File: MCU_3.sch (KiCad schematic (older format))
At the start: 18 parts, among them U2 STM32F051K6Ux

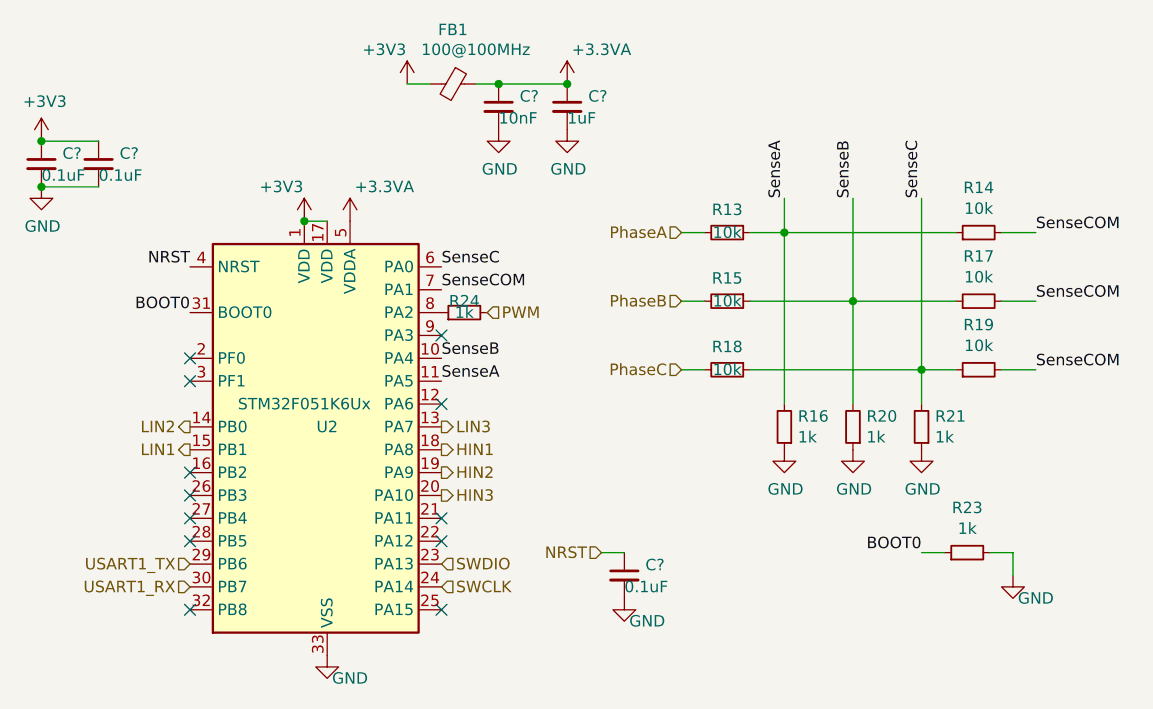
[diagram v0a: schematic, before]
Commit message: Added the rest of the phases and their associated components
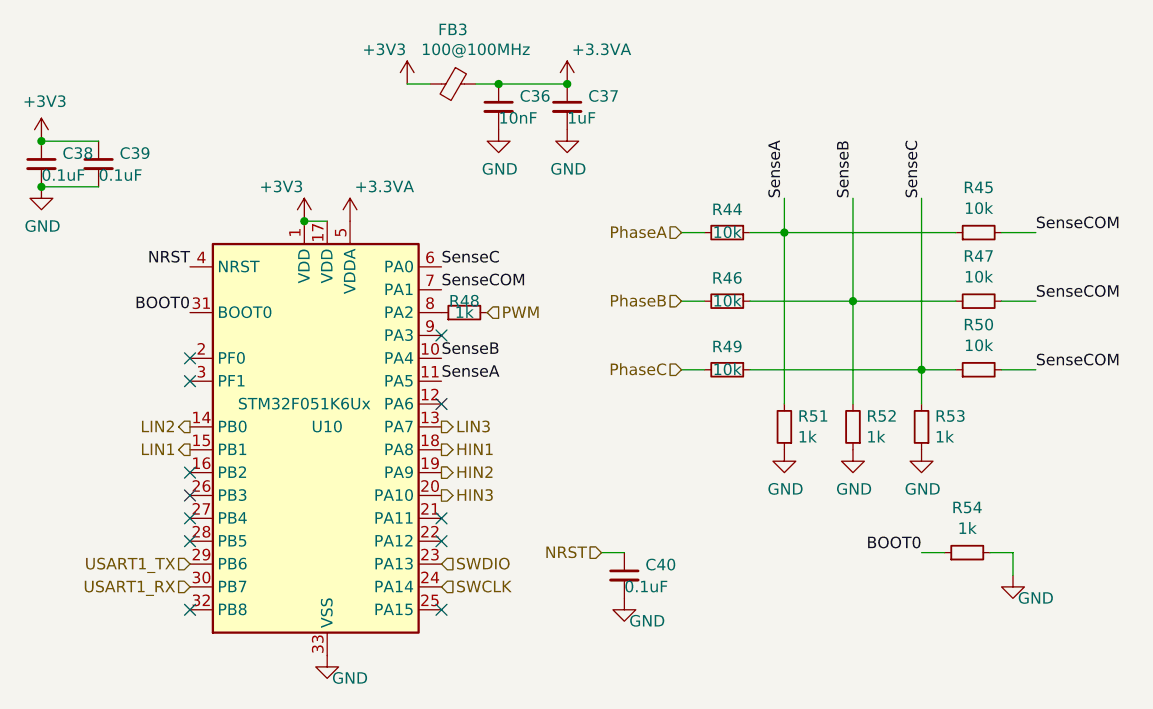
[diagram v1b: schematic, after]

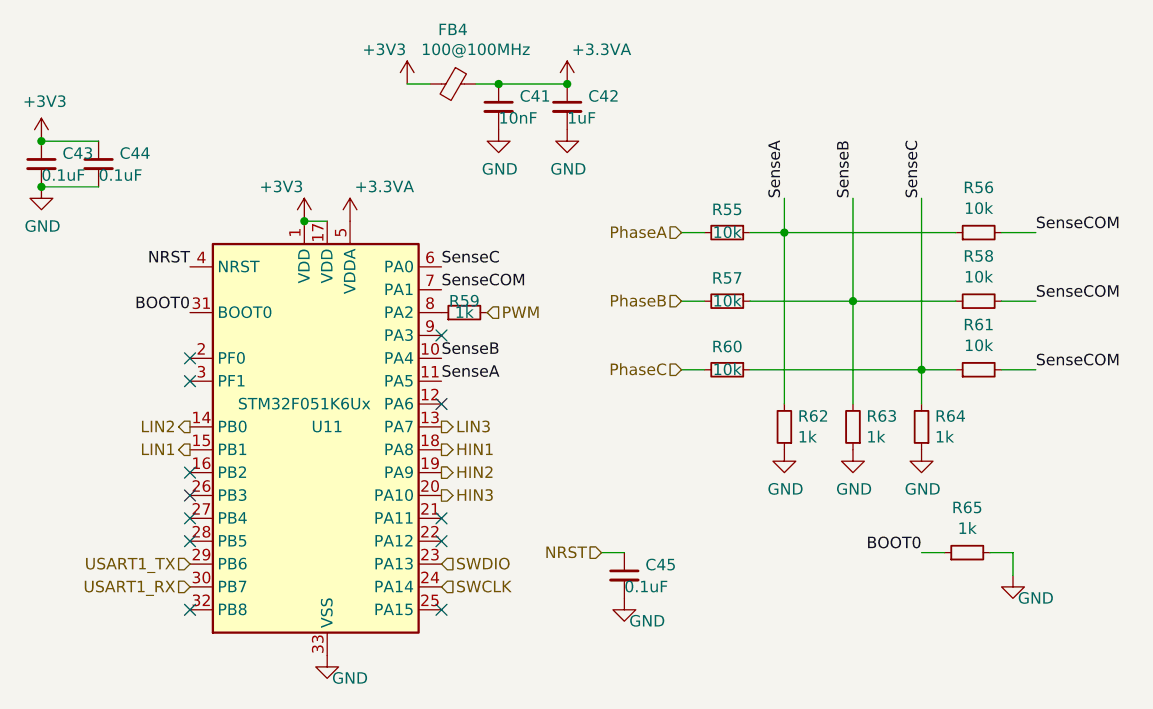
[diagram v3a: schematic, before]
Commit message: Finalized back layer and added FETs to front layer
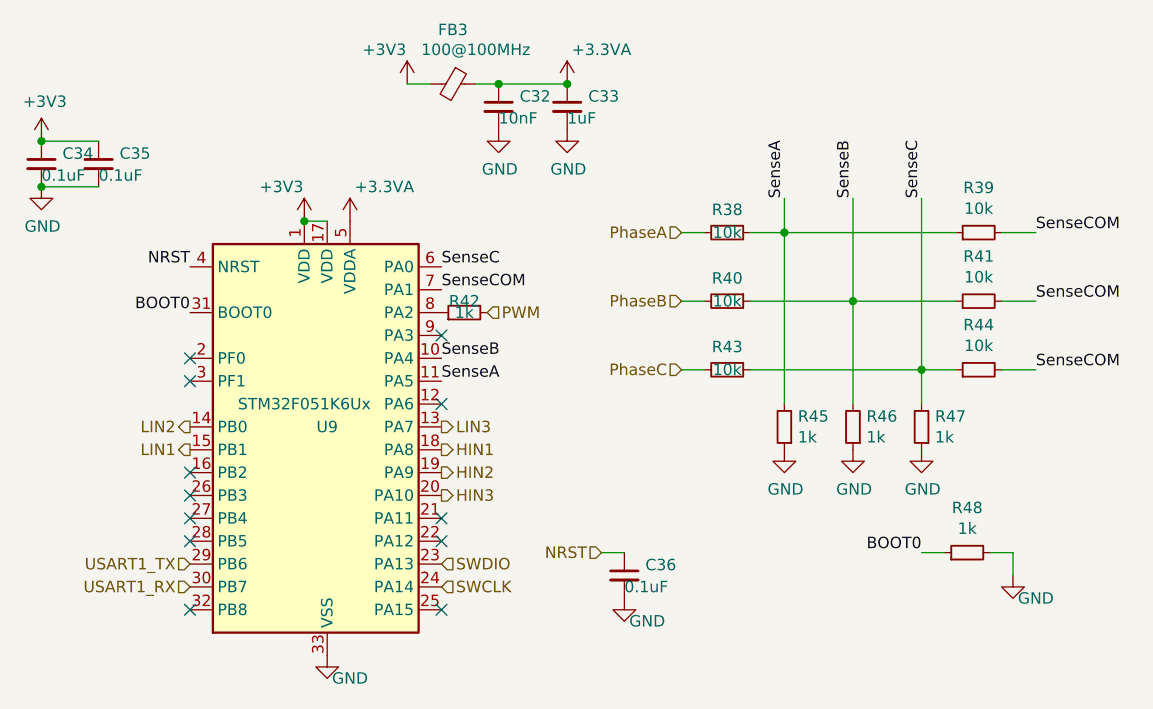
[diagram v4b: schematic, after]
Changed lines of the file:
@@
 AR Path="/60535FFC/605D8EB1" Ref="U9"  Part="1"
 AR Path="/6055186B/605D8EB1" Ref="U11"  Part="1"
-F 0 "U11" H 5050 2950 50  0000 C CNN
+F 0 "U9" H 5050 2950 50  0000 C CNN
 F 1 "STM32F051K6Ux" H 4950 3050 50  0000 C CNN
 F 2 "Package_DFN_QFN:QFN-32-1EP_5x5mm_P0.5mm_EP3.45x3.45mm" H 4550 2050 50  0001 R CNN
@@
 AR Path="/60535FFC/605D8EC0" Ref="#PWR0178"  Part="1"
 AR Path="/6055186B/605D8EC0" Ref="#PWR0205"  Part="1"
-F 0 "#PWR0205" H 4950 1900 50  0001 C CNN
+F 0 "#PWR0178" H 4950 1900 50  0001 C CNN
 F 1 "+3V3" H 4850 2200 50  0000 C CNN
 F 2 "" H 4950 2050 50  0001 C CNN
@@
 AR Path="/60535FFC/60305B97" Ref="#PWR0179"  Part="1"
 AR Path="/6055186B/60305B97" Ref="#PWR0206"  Part="1"
-F 0 "#PWR0206" H 5050 3700 50  0001 C CNN
+F 0 "#PWR0179" H 5050 3700 50  0001 C CNN
 F 1 "GND" H 5150 3850 50  0000 C CNN
 F 2 "" H 5050 3950 50  0001 C CNN
@@
 AR Path="/60535FFC/605D8EC1" Ref="C34"  Part="1"
 AR Path="/6055186B/605D8EC1" Ref="C43"  Part="1"
-F 0 "C43" H 3892 1846 50  0000 L CNN
+F 0 "C34" H 3892 1846 50  0000 L CNN
 F 1 "0.1uF" H 3800 1750 50  0000 L CNN
 F 2 "Capacitor_SMD:C_0402_1005Metric" H 3800 1800 50  0001 C CNN
@@
 AR Path="/60535FFC/60308078" Ref="#PWR0180"  Part="1"
 AR Path="/6055186B/60308078" Ref="#PWR0207"  Part="1"
-F 0 "#PWR0207" H 3800 1550 50  0001 C CNN
+F 0 "#PWR0180" H 3800 1550 50  0001 C CNN
 F 1 "+3V3" H 3815 1873 50  0000 C CNN
 F 2 "" H 3800 1700 50  0001 C CNN
@@
 AR Path="/60535FFC/6030807E" Ref="#PWR0181"  Part="1"
 AR Path="/6055186B/6030807E" Ref="#PWR0208"  Part="1"
-F 0 "#PWR0208" H 3800 1650 50  0001 C CNN
+F 0 "#PWR0181" H 3800 1650 50  0001 C CNN
 F 1 "GND" H 3805 1727 50  0000 C CNN
 F 2 "" H 3800 1900 50  0001 C CNN
@@
 AR Path="/60535FFC/60308088" Ref="C32"  Part="1"
 AR Path="/6055186B/60308088" Ref="C41"  Part="1"
-F 0 "C41" H 5892 1596 50  0000 L CNN
+F 0 "C32" H 5892 1596 50  0000 L CNN
 F 1 "10nF" H 5800 1500 50  0000 L CNN
 F 2 "Capacitor_SMD:C_0402_1005Metric" H 5800 1550 50  0001 C CNN
@@
 AR Path="/60535FFC/605D8EAF" Ref="C35"  Part="1"
 AR Path="/6055186B/605D8EAF" Ref="C44"  Part="1"
-F 0 "C44" H 4142 1846 50  0000 L CNN
+F 0 "C35" H 4142 1846 50  0000 L CNN
 F 1 "0.1uF" H 4050 1750 50  0000 L CNN
 F 2 "Capacitor_SMD:C_0402_1005Metric" H 4050 1800 50  0001 C CNN
@@
 AR Path="/60535FFC/605D8EB8" Ref="R45"  Part="1"
 AR Path="/6055186B/605D8EB8" Ref="R62"  Part="1"
-F 0 "R62" H 6991 2904 50  0000 R CNN
+F 0 "R45" H 6991 2904 50  0000 R CNN
 F 1 "1k" H 6991 2995 50  0000 R CNN
 F 2 "Resistor_SMD:R_0402_1005Metric" H 7050 2950 50  0001 C CNN
@@
 AR Path="/60535FFC/605D8EB9" Ref="#PWR0182"  Part="1"
 AR Path="/6055186B/605D8EB9" Ref="#PWR0209"  Part="1"
-F 0 "#PWR0209" H 7050 2800 50  0001 C CNN
+F 0 "#PWR0182" H 7050 2800 50  0001 C CNN
 F 1 "GND" H 7055 2877 50  0000 C CNN
 F 2 "" H 7050 3050 50  0001 C CNN
@@
 AR Path="/60535FFC/605D8EB7" Ref="R38"  Part="1"
 AR Path="/6055186B/605D8EB7" Ref="R55"  Part="1"
-F 0 "R55" V 6700 2100 50  0000 C CNN
+F 0 "R38" V 6700 2100 50  0000 C CNN
 F 1 "10k" V 6800 2100 50  0000 C CNN
 F 2 "Resistor_SMD:R_0402_1005Metric" H 6800 2100 50  0001 C CNN
@@
 AR Path="/60535FFC/605D8EBA" Ref="R39"  Part="1"
 AR Path="/6055186B/605D8EBA" Ref="R56"  Part="1"
-F 0 "R56" V 8096 2100 50  0000 C CNN
+F 0 "R39" V 8096 2100 50  0000 C CNN
 F 1 "10k" V 8005 2100 50  0000 C CNN
 F 2 "Resistor_SMD:R_0402_1005Metric" H 7900 2100 50  0001 C CNN
@@
 AR Path="/60535FFC/6050F9A7" Ref="R40"  Part="1"
 AR Path="/6055186B/6050F9A7" Ref="R57"  Part="1"
-F 0 "R57" V 6700 2400 50  0000 C CNN
+F 0 "R40" V 6700 2400 50  0000 C CNN
 F 1 "10k" V 6800 2400 50  0000 C CNN
 F 2 "Resistor_SMD:R_0402_1005Metric" H 6800 2400 50  0001 C CNN
@@
 AR Path="/60535FFC/6050F9A8" Ref="R43"  Part="1"
 AR Path="/6055186B/6050F9A8" Ref="R60"  Part="1"
-F 0 "R60" V 6700 2700 50  0000 C CNN
+F 0 "R43" V 6700 2700 50  0000 C CNN
 F 1 "10k" V 6800 2700 50  0000 C CNN
 F 2 "Resistor_SMD:R_0402_1005Metric" H 6800 2700 50  0001 C CNN
@@
 AR Path="/60535FFC/605D8EC2" Ref="R46"  Part="1"
 AR Path="/6055186B/605D8EC2" Ref="R63"  Part="1"
-F 0 "R63" H 7291 2904 50  0000 R CNN
+F 0 "R46" H 7291 2904 50  0000 R CNN
 F 1 "1k" H 7291 2995 50  0000 R CNN
 F 2 "Resistor_SMD:R_0402_1005Metric" H 7350 2950 50  0001 C CNN
@@
 AR Path="/60535FFC/605D8EC3" Ref="R47"  Part="1"
 AR Path="/6055186B/605D8EC3" Ref="R64"  Part="1"
-F 0 "R64" H 7591 2904 50  0000 R CNN
+F 0 "R47" H 7591 2904 50  0000 R CNN
 F 1 "1k" H 7591 2995 50  0000 R CNN
 F 2 "Resistor_SMD:R_0402_1005Metric" H 7650 2950 50  0001 C CNN
@@
 AR Path="/60535FFC/605D8EC4" Ref="R41"  Part="1"
 AR Path="/6055186B/605D8EC4" Ref="R58"  Part="1"
-F 0 "R58" V 8096 2400 50  0000 C CNN
+F 0 "R41" V 8096 2400 50  0000 C CNN
 F 1 "10k" V 8005 2400 50  0000 C CNN
 F 2 "Resistor_SMD:R_0402_1005Metric" H 7900 2400 50  0001 C CNN
@@
 AR Path="/60535FFC/605D8EC5" Ref="R44"  Part="1"
 AR Path="/6055186B/605D8EC5" Ref="R61"  Part="1"
-F 0 "R61" V 8096 2700 50  0000 C CNN
+F 0 "R44" V 8096 2700 50  0000 C CNN
 F 1 "10k" V 8005 2700 50  0000 C CNN
 F 2 "Resistor_SMD:R_0402_1005Metric" H 7900 2700 50  0001 C CNN
@@
 AR Path="/60535FFC/605D8EC6" Ref="#PWR0183"  Part="1"
 AR Path="/6055186B/605D8EC6" Ref="#PWR0210"  Part="1"
-F 0 "#PWR0210" H 7350 2800 50  0001 C CNN
+F 0 "#PWR0183" H 7350 2800 50  0001 C CNN
 F 1 "GND" H 7355 2877 50  0000 C CNN
 F 2 "" H 7350 3050 50  0001 C CNN
@@
 AR Path="/60535FFC/605D8EBB" Ref="#PWR0184"  Part="1"
 AR Path="/6055186B/605D8EBB" Ref="#PWR0211"  Part="1"
-F 0 "#PWR0211" H 7650 2800 50  0001 C CNN
+F 0 "#PWR0184" H 7650 2800 50  0001 C CNN
 F 1 "GND" H 7655 2877 50  0000 C CNN
 F 2 "" H 7650 3050 50  0001 C CNN
@@
 AR Path="/60535FFC/605D8EB4" Ref="#PWR0185"  Part="1"
 AR Path="/6055186B/605D8EB4" Ref="#PWR0212"  Part="1"
-F 0 "#PWR0212" H 6350 3450 50  0001 C CNN
+F 0 "#PWR0185" H 6350 3450 50  0001 C CNN
 F 1 "GND" H 6450 3600 50  0000 C CNN
 F 2 "" H 6350 3700 50  0001 C CNN
@@
 AR Path="/60535FFC/605D8EB5" Ref="R48"  Part="1"
 AR Path="/6055186B/605D8EB5" Ref="R65"  Part="1"
-F 0 "R65" V 8046 3500 50  0000 C CNN
+F 0 "R48" V 8046 3500 50  0000 C CNN
 F 1 "1k" V 7955 3500 50  0000 C CNN
 F 2 "Resistor_SMD:R_0402_1005Metric" H 7850 3500 50  0001 C CNN
@@
 AR Path="/60535FFC/605D8EB6" Ref="#PWR0186"  Part="1"
 AR Path="/6055186B/605D8EB6" Ref="#PWR0213"  Part="1"
-F 0 "#PWR0213" H 8050 3350 50  0001 C CNN
+F 0 "#PWR0186" H 8050 3350 50  0001 C CNN
 F 1 "GND" H 8150 3500 50  0000 C CNN
 F 2 "" H 8050 3600 50  0001 C CNN
@@
 AR Path="/60535FFC/605D8EC7" Ref="R42"  Part="1"
 AR Path="/6055186B/605D8EC7" Ref="R59"  Part="1"
-F 0 "R59" V 5700 2450 50  0000 C CNN
+F 0 "R42" V 5700 2450 50  0000 C CNN
 F 1 "1k" V 5650 2450 50  0000 C CNN
 F 2 "Resistor_SMD:R_0402_1005Metric" H 5650 2450 50  0001 C CNN
@@
 AR Path="/60535FFC/605D8EC8" Ref="C36"  Part="1"
 AR Path="/6055186B/605D8EC8" Ref="C45"  Part="1"
-F 0 "C45" H 6442 3646 50  0000 L CNN
+F 0 "C36" H 6442 3646 50  0000 L CNN
 F 1 "0.1uF" H 6350 3550 50  0000 L CNN
 F 2 "Capacitor_SMD:C_0402_1005Metric" H 6350 3600 50  0001 C CNN
@@
 AR Path="/60535FFC/6059DC49" Ref="#PWR0187"  Part="1"
 AR Path="/6055186B/6059DC49" Ref="#PWR0214"  Part="1"
-F 0 "#PWR0214" H 5150 1900 50  0001 C CNN
+F 0 "#PWR0187" H 5150 1900 50  0001 C CNN
 F 1 "+3.3VA" H 5300 2200 50  0000 C CNN
 F 2 "" H 5150 2050 50  0001 C CNN
@@
 AR Path="/60535FFC/605D8EB0" Ref="#PWR0188"  Part="1"
 AR Path="/6055186B/605D8EB0" Ref="#PWR0219"  Part="1"
-F 0 "#PWR0219" H 5400 1300 50  0001 C CNN
+F 0 "#PWR0188" H 5400 1300 50  0001 C CNN
 F 1 "+3V3" H 5300 1600 50  0000 C CNN
 F 2 "" H 5400 1450 50  0001 C CNN
@@
 AR Path="/60535FFC/605D8EBC" Ref="#PWR0189"  Part="1"
 AR Path="/6055186B/605D8EBC" Ref="#PWR0220"  Part="1"
-F 0 "#PWR0220" H 6100 1300 50  0001 C CNN
+F 0 "#PWR0189" H 6100 1300 50  0001 C CNN
 F 1 "+3.3VA" H 6250 1600 50  0000 C CNN
 F 2 "" H 6100 1450 50  0001 C CNN
@@
 AR Path="/60535FFC/605D8EBD" Ref="C33"  Part="1"
 AR Path="/6055186B/605D8EBD" Ref="C42"  Part="1"
-F 0 "C42" H 6192 1596 50  0000 L CNN
+F 0 "C33" H 6192 1596 50  0000 L CNN
 F 1 "1uF" H 6100 1500 50  0000 L CNN
 F 2 "Capacitor_SMD:C_0402_1005Metric" H 6100 1550 50  0001 C CNN
@@
 AR Path="/60535FFC/605D8EBE" Ref="FB3"  Part="1"
 AR Path="/6055186B/605D8EBE" Ref="FB4"  Part="1"
-F 0 "FB4" V 5363 1450 50  0000 C CNN
+F 0 "FB3" V 5363 1450 50  0000 C CNN
 F 1 "100@100MHz" V 5450 1550 50  0000 C CNN
 F 2 "Inductor_SMD:L_0603_1608Metric" V 5530 1450 50  0001 C CNN
@@
 AR Path="/60535FFC/605D8EBF" Ref="#PWR0190"  Part="1"
 AR Path="/6055186B/605D8EBF" Ref="#PWR0221"  Part="1"
-F 0 "#PWR0221" H 6100 1400 50  0001 C CNN
+F 0 "#PWR0190" H 6100 1400 50  0001 C CNN
 F 1 "GND" H 6105 1477 50  0000 C CNN
 F 2 "" H 6100 1650 50  0001 C CNN
@@
 AR Path="/60535FFC/6059DC4A" Ref="#PWR0191"  Part="1"
 AR Path="/6055186B/6059DC4A" Ref="#PWR0222"  Part="1"
-F 0 "#PWR0222" H 5800 1400 50  0001 C CNN
+F 0 "#PWR0191" H 5800 1400 50  0001 C CNN
 F 1 "GND" H 5805 1477 50  0000 C CNN
 F 2 "" H 5800 1650 50  0001 C CNN

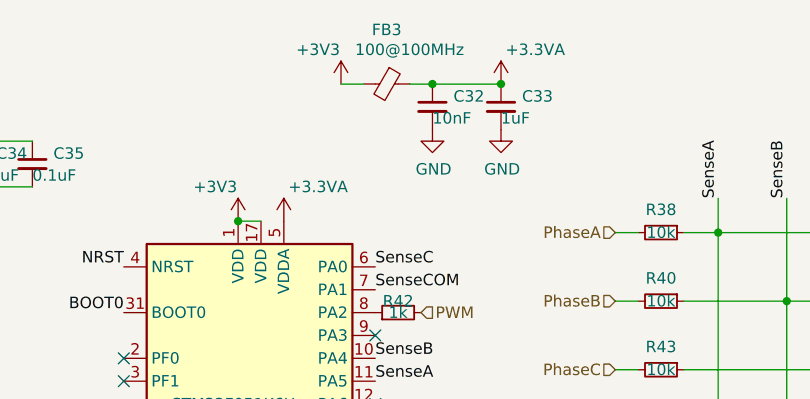
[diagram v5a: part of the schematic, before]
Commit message: Finished all traces and vias
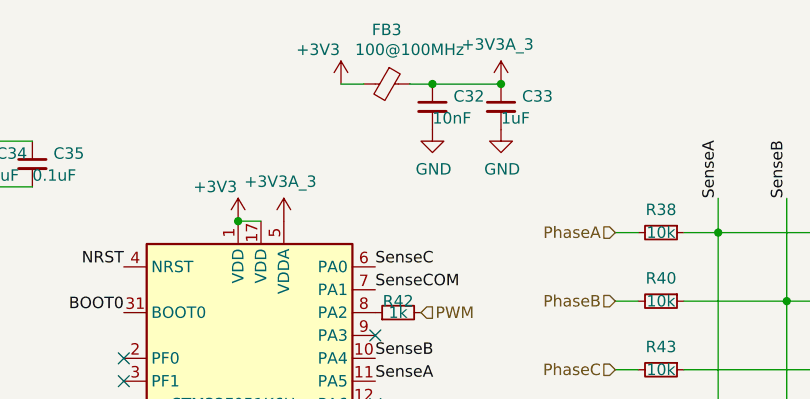
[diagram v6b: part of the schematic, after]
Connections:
- net +3.3VA renamed +3.3VA_3
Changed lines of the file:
@@
 NRST
-$Comp
-L power:+3.3VA #PWR0109
-U 1 1 6059DC49
-P 5150 2050
-AR Path="/60302A40/6059DC49" Ref="#PWR0109"  Part="1"
-AR Path="/605793E5/6059DC49" Ref="#PWR0156"  Part="1"
-AR Path="/6057AB62/6059DC49" Ref="#PWR0185"  Part="1"
-AR Path="/60597D10/6059DC49" Ref="#PWR?"  Part="1"
-AR Path="/60568CD3/6059DC49" Ref="#PWR0200"  Part="1"
-AR Path="/60595215/6059DC49" Ref="#PWR0200"  Part="1"
-AR Path="/605CA831/6059DC49" Ref="#PWR0200"  Part="1"
-AR Path="/605DC779/6059DC49" Ref="#PWR0229"  Part="1"
-AR Path="/60535FFC/6059DC49" Ref="#PWR0187"  Part="1"
-AR Path="/6055186B/6059DC49" Ref="#PWR0214"  Part="1"
-F 0 "#PWR0187" H 5150 1900 50  0001 C CNN
-F 1 "+3.3VA" H 5300 2200 50  0000 C CNN
-F 2 "" H 5150 2050 50  0001 C CNN
-F 3 "" H 5150 2050 50  0001 C CNN
-	1    5150 2050
-	1    0    0    -1
-$EndComp
 $Comp
 L power:+3V3 #PWR0110
@@
 F 3 "" H 5400 1450 50  0001 C CNN
 	1    5400 1450
-	1    0    0    -1
-$EndComp
-$Comp
-L power:+3.3VA #PWR0111
-U 1 1 605D8EBC
-P 6100 1450
-AR Path="/60302A40/605D8EBC" Ref="#PWR0111"  Part="1"
-AR Path="/605793E5/605D8EBC" Ref="#PWR0158"  Part="1"
-AR Path="/6057AB62/605D8EBC" Ref="#PWR0187"  Part="1"
-AR Path="/60597D10/605D8EBC" Ref="#PWR?"  Part="1"
-AR Path="/60568CD3/605D8EBC" Ref="#PWR0202"  Part="1"
-AR Path="/60595215/605D8EBC" Ref="#PWR0202"  Part="1"
-AR Path="/605CA831/605D8EBC" Ref="#PWR0202"  Part="1"
-AR Path="/605DC779/605D8EBC" Ref="#PWR0231"  Part="1"
-AR Path="/60535FFC/605D8EBC" Ref="#PWR0189"  Part="1"
-AR Path="/6055186B/605D8EBC" Ref="#PWR0220"  Part="1"
-F 0 "#PWR0189" H 6100 1300 50  0001 C CNN
-F 1 "+3.3VA" H 6250 1600 50  0000 C CNN
-F 2 "" H 6100 1450 50  0001 C CNN
-F 3 "" H 6100 1450 50  0001 C CNN
-	1    6100 1450
 	1    0    0    -1
 $EndComp
@@
 Wire Wire Line
 	5700 1450 5800 1450
-Connection ~ 6100 1450
 Wire Wire Line
 	5800 1450 6100 1450
@@
 Text HLabel 4450 3550 0    50   Input ~ 0
 USART1_TX
+$Comp
+L power:+3V3A_3 #PWR0156
+U 1 1 60567D72
+P 5150 2050
+F 0 "#PWR0156" H 5150 2000 50  0001 C CNN
+F 1 "+3V3A_3" H 5135 2223 50  0000 C CNN
+F 2 "" H 5150 2050 50  0001 C CNN
+F 3 "" H 5150 2050 50  0001 C CNN
+	1    5150 2050
+	1    0    0    -1
+$EndComp
+$Comp
+L power:+3V3A_3 #PWR?
+U 1 1 6056C29D
+P 6100 1450
+F 0 "#PWR?" H 6100 1400 50  0001 C CNN
+F 1 "+3V3A_3" H 6085 1623 50  0000 C CNN
+F 2 "" H 6100 1450 50  0001 C CNN
+F 3 "" H 6100 1450 50  0001 C CNN
+	1    6100 1450
+	1    0    0    -1
+$EndComp
+Connection ~ 6100 1450
 $EndSCHEMATC
